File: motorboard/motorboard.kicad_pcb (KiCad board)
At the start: 2 copper layers, 94 x 94 mm, 72 parts, among them J1 Stepper, J2 USB_B_Micro, J3 DC Motor, J4 LiPo, J5 UART, J6 Encoders, J7 ICSP, J8 Separate LiPo, Q1 PMV20ENR, U1 TB6612FNG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

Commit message: forgot something crucial...
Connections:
- U2 pad 28: Net-(U2-Pad28) -> STEP
- U2 pad 29: Net-(U2-Pad29) -> DIR
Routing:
- net STEP: track 0.00 -> 26.3 mm, vias 0 -> 2
- net DIR: track 0.00 -> 24.8 mm, vias 0 -> 2

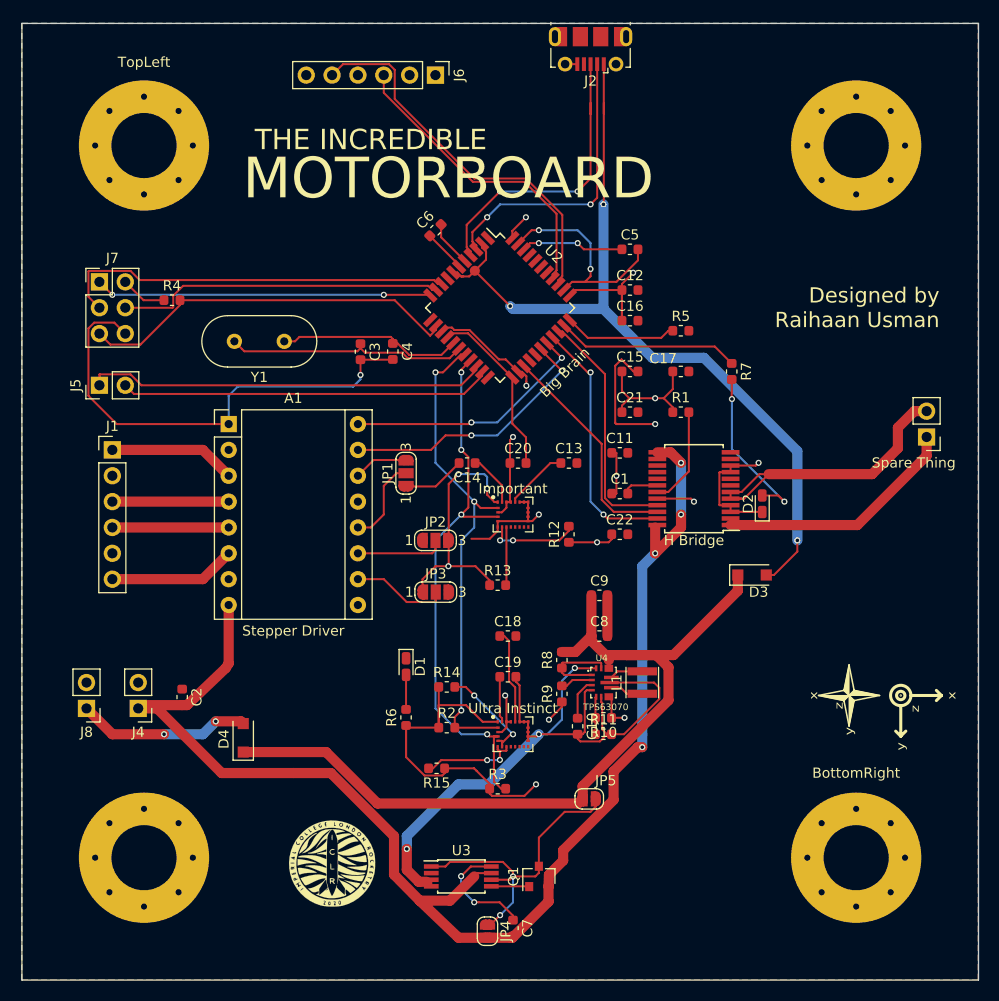
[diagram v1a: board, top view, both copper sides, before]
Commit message: moved things around, looks cleaner
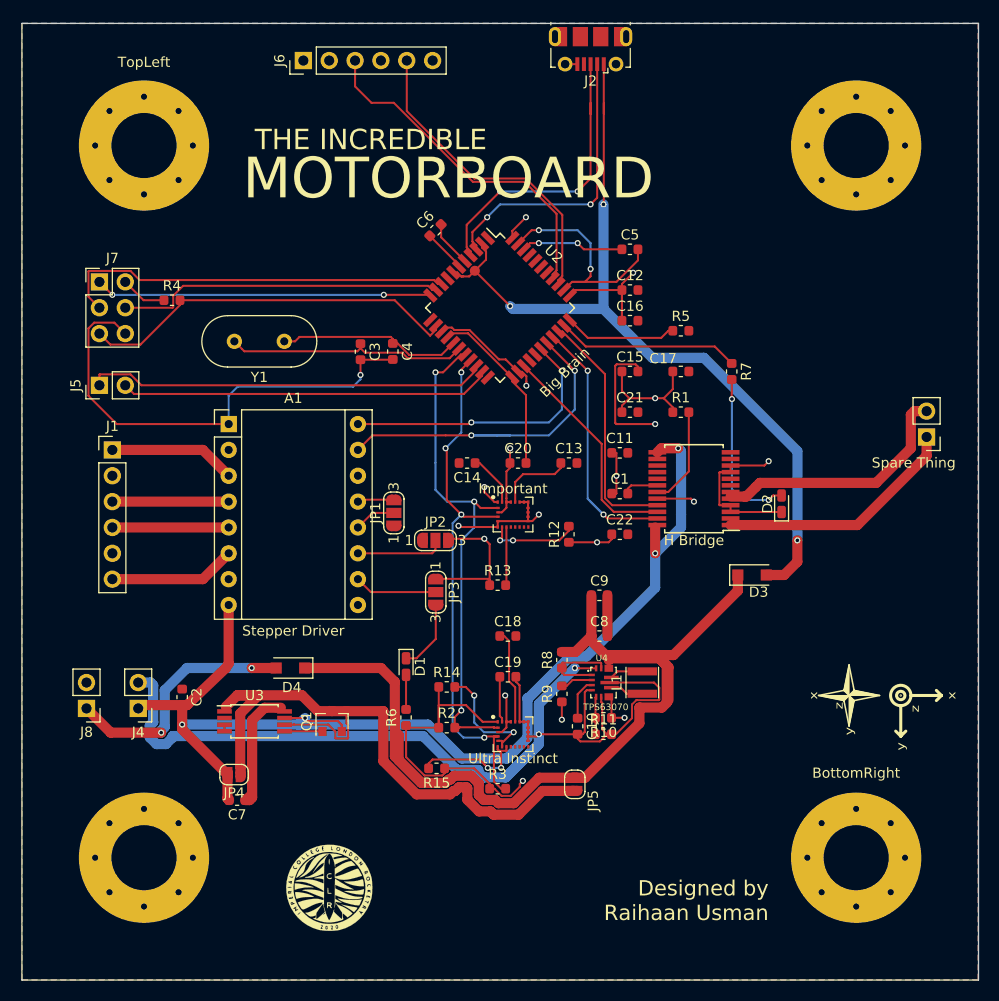
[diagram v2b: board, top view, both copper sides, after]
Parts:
- moved C7 29.9 mm to (116.4, 127.1), turned to 180 degrees
- moved JP4 29.3 mm to (116.1, 124.6), turned to 180 degrees
- moved Q1 25.4 mm to (125.7, 119.4)
- moved U3 25.4 mm to (118.1, 119.4)
- moved J6 13.1 mm to (122.9, 54.5), turned to 90 degrees
- moved D4 8.28 mm to (121.6, 114.1), turned to 180 degrees
- moved JP1 4.08 mm to (131.8, 98.9)
- moved G*** 2.40 mm to (125.5, 135.7)
- moved JP5 2.02 mm to (149.6, 125.6), turned to 270 degrees
- moved D2 1.90 mm to (169.9, 98.0)
- turned JP3 to 270 degrees
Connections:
- U2 pad 28: STEP -> DIR
- U2 pad 29: DIR -> STEP
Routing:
- net Net-(JP4-Pad1): track 31.0 -> 72.5 mm, vias 2 -> 0
- net GND: track 223.4 -> 252.6 mm
- net +15V: track 135.3 -> 113.7 mm
- net VDD: track 86.0 -> 104.4 mm
- net +3V3: track 146.1 -> 132.6 mm, vias 15 -> 14
- net STEP: track 26.3 -> 34.4 mm
- net Net-(C7-Pad1): track 11.3 -> 18.8 mm, vias 2 -> 0
- net Net-(D4-Pad2): track 17.1 -> 24.5 mm
- net A2: track 37.8 -> 31.4 mm
- net AO2: track 30.5 -> 25.3 mm
- net A1: track 30.1 -> 35.2 mm
- net MS3: track 8.59 -> 4.12 mm
- net DIR: track 24.8 -> 27.4 mm
- net PWMA: track 25.1 -> 26.8 mm
- net Net-(R14-Pad2): track 10.4 -> 12.1 mm
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
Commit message: rev2 started
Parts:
- J4: footprint Connector_PinHeader_2.54mm:PinHeader_1x02_P2.54mm_Vertical -> xt30:AMASS_XT30UPB-F_1x02_P5.0mm_Vertical
- moved J8 18.2 mm to (98.8, 100.2)
- moved J4 3.03 mm to (103.9, 119.2), turned to 90 degrees
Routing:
- net GND: track 252.6 -> 234.4 mm, vias 9 -> 10
- net Net-(D4-Pad2): track 24.5 -> 30.2 mm, vias 2 -> 1
- net +15V: track 113.7 -> 117.9 mm
- net Net-(JP4-Pad1): track 72.5 -> 75.9 mm
- net VDD: track 104.4 -> 103.2 mm
- net RST: track 37.7 -> 38.9 mm

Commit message: nicer board!
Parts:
- Y1: footprint Crystal:Crystal_HC18-U_Vertical -> Crystal:Crystal_HC49-4H_Vertical
- moved REF** 2.87 mm to (179.6, 114.8)
- moved REF** 2.87 mm to (174.5, 114.8)
- moved R4 1.38 mm to (110.2, 79.4), turned to 270 degrees
- moved JP3 1.18 mm to (135.9, 105.5), turned to 180 degrees
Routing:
- net Net-(JP4-Pad1): track 75.9 -> 70.6 mm
- net +3V3: track 132.8 -> 128.9 mm, vias 14 -> 15
- net GND: track 234.4 -> 236.8 mm, vias 10 -> 12
- net RST: track 38.9 -> 36.7 mm
- net VDD: track 103.2 -> 101.5 mm
- net MS1: track 8.18 -> 9.19 mm
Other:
- board text added: "Electronics & Payload"
- board text added: "Imperial College London Rocketry"
- board text added: "REV 2"
- board text added: "Redstone Powered..."
- board text added: "The Motorboard is the payload controller designed for HMSS Sporadic Impulse Designed to drive a motor & pulley system to maintain the orientation of the payload cameras!"
- board text added: "What Do I Do?"
- board text removed: "Redstone Powered"

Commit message: Rev2 complete
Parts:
- moved TopLeft 0.21 mm to (107.2, 62.6)
- moved TopRight 0.20 mm to (177.2, 62.6)
- moved BottomLeft 0.19 mm to (107.2, 132.6)
- moved e 0.18 mm to (177.2, 132.6)
- renumbered BottomRight to e
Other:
- outline, holes or cut-outs redrawn
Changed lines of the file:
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@@
   (general
     (thickness 1.6)
-    (drawings 19)
+    (drawings 23)
     (tracks 766)
     (zones 0)
@@
     (mod_text_size 1 1)
     (mod_text_width 0.15)
-    (pad_size 1.524 1.524)
-    (pad_drill 0.762)
+    (pad_size 12.8 12.8)
+    (pad_drill 6.4)
     (pad_to_mask_clearance 0.051)
     (solder_mask_min_width 0.25)
@@
     (uvia_drill 0.1)
   )
+  (module MountingHole:MountingHole_6.4mm_M6_Pad_Via placed (layer F.Cu)
+    (at 177.2 132.6)
+    (descr "Mounting Hole 6.4mm, M6")
+    (tags "mounting hole 6.4mm m6")
+    (attr virtual)
+    (fp_text reference e (at 0 -8.32) (layer F.Fab)
+      (effects (font (size 1 1) (thickness 0.15)))
+    )
+    (fp_text value Yeet (at 0 7.4) (layer F.Fab)
+      (effects (font (size 1 1) (thickness 0.15)))
+    )
+    (fp_text user %R (at 0.3 0) (layer F.Fab)
+      (effects (font (size 1 1) (thickness 0.15)))
+    )
+    (fp_circle (center 0 0) (end 6.4 0) (layer Cmts.User) (width 0.15))
+    (fp_circle (center 0 0) (end 6.65 0) (layer F.CrtYd) (width 0.05))
+    (pad 1 thru_hole circle (at 0 0) (size 12.8 12.8) (drill 6.4) (layers *.Cu *.Mask))
+    (pad 1 thru_hole circle (at 4.8 0) (size 0.9 0.9) (drill 0.6) (layers *.Cu *.Mask))
+    (pad 1 thru_hole circle (at 3.394113 3.394113) (size 0.9 0.9) (drill 0.6) (layers *.Cu *.Mask))
+    (pad 1 thru_hole circle (at 0 4.8) (size 0.9 0.9) (drill 0.6) (layers *.Cu *.Mask))
+    (pad 1 thru_hole circle (at -3.394113 3.394113) (size 0.9 0.9) (drill 0.6) (layers *.Cu *.Mask))
+    (pad 1 thru_hole circle (at -4.8 0) (size 0.9 0.9) (drill 0.6) (layers *.Cu *.Mask))
+    (pad 1 thru_hole circle (at -3.394113 -3.394113) (size 0.9 0.9) (drill 0.6) (layers *.Cu *.Mask))
+    (pad 1 thru_hole circle (at 0 -4.8) (size 0.9 0.9) (drill 0.6) (layers *.Cu *.Mask))
+    (pad 1 thru_hole circle (at 3.394113 -3.394113) (size 0.9 0.9) (drill 0.6) (layers *.Cu *.Mask))
+  )
   (module Crystal:Crystal_HC49-4H_Vertical (layer F.Cu)
     (at 121.031 82.042 180)
@@
   )
   (module MountingHole:MountingHole_6.4mm_M6_Pad_Via placed (layer F.Cu)
-    (at 177.23 132.78)
-    (descr "Mounting Hole 6.4mm, M6")
-    (tags "mounting hole 6.4mm m6")
-    (attr virtual)
-    (fp_text reference BottomRight (at 0 -8.32) (layer F.SilkS)
-      (effects (font (size 1 1) (thickness 0.15)))
-    )
-    (fp_text value Yeet (at 0 7.4) (layer F.Fab)
-      (effects (font (size 1 1) (thickness 0.15)))
-    )
-    (fp_text user %R (at 0.3 0) (layer F.Fab)
-      (effects (font (size 1 1) (thickness 0.15)))
-    )
-    (fp_circle (center 0 0) (end 6.4 0) (layer Cmts.User) (width 0.15))
-    (fp_circle (center 0 0) (end 6.65 0) (layer F.CrtYd) (width 0.05))
-    (pad 1 thru_hole circle (at 0 0) (size 12.8 12.8) (drill 6.4) (layers *.Cu *.Mask))
-    (pad 1 thru_hole circle (at 4.8 0) (size 0.9 0.9) (drill 0.6) (layers *.Cu *.Mask))
-    (pad 1 thru_hole circle (at 3.394113 3.394113) (size 0.9 0.9) (drill 0.6) (layers *.Cu *.Mask))
-    (pad 1 thru_hole circle (at 0 4.8) (size 0.9 0.9) (drill 0.6) (layers *.Cu *.Mask))
-    (pad 1 thru_hole circle (at -3.394113 3.394113) (size 0.9 0.9) (drill 0.6) (layers *.Cu *.Mask))
-    (pad 1 thru_hole circle (at -4.8 0) (size 0.9 0.9) (drill 0.6) (layers *.Cu *.Mask))
-    (pad 1 thru_hole circle (at -3.394113 -3.394113) (size 0.9 0.9) (drill 0.6) (layers *.Cu *.Mask))
-    (pad 1 thru_hole circle (at 0 -4.8) (size 0.9 0.9) (drill 0.6) (layers *.Cu *.Mask))
-    (pad 1 thru_hole circle (at 3.394113 -3.394113) (size 0.9 0.9) (drill 0.6) (layers *.Cu *.Mask))
-  )
-  (module MountingHole:MountingHole_6.4mm_M6_Pad_Via placed (layer F.Cu)
-    (at 177.23 62.8)
+    (at 177.2 62.6)
     (descr "Mounting Hole 6.4mm, M6")
     (tags "mounting hole 6.4mm m6")
@@
   )
   (module MountingHole:MountingHole_6.4mm_M6_Pad_Via placed (layer F.Cu)
-    (at 107.25 62.8)
+    (at 107.2 62.6)
     (descr "Mounting Hole 6.4mm, M6")
     (tags "mounting hole 6.4mm m6")
@@
   )
   (module MountingHole:MountingHole_6.4mm_M6_Pad_Via placed (layer F.Cu)
-    (at 107.25 132.78)
+    (at 107.2 132.6)
     (descr "Mounting Hole 6.4mm, M6")
     (tags "mounting hole 6.4mm m6")
@@
     )
   )
+  (gr_arc (start 107.200001 132.600001) (end 95.200001 132.600001) (angle -90) (layer Edge.Cuts) (width 0.2))
+  (gr_line (start 95.200001 132.600001) (end 95.200001 62.600001) (layer Edge.Cuts) (width 0.2))
+  (gr_line (start 107.200001 50.600001) (end 177.199999 50.600002) (layer Edge.Cuts) (width 0.2))
+  (gr_arc (start 107.200001 62.600002) (end 107.200001 50.600001) (angle -90) (layer Edge.Cuts) (width 0.2))
+  (gr_line (start 177.2 144.6) (end 107.200001 144.600001) (layer Edge.Cuts) (width 0.2))
+  (gr_arc (start 177.199999 62.600002) (end 189.199999 62.600002) (angle -90) (layer Edge.Cuts) (width 0.2))
+  (gr_line (start 189.199999 62.600002) (end 189.2 132.6) (layer Edge.Cuts) (width 0.2))
+  (gr_arc (start 177.2 132.6) (end 177.2 144.6) (angle -90) (layer Edge.Cuts) (width 0.2))
   (gr_text "What Do I Do?" (at 142.468 135.476) (layer B.SilkS)
     (effects (font (size 1.5 1.5) (thickness 0.3)) (justify mirror))
@@
     (effects (font (size 1.5 1.5) (thickness 0.3)) (justify right))
   )
-  (gr_line (start 189.25 144.8) (end 95.25 144.8) (layer Edge.Cuts) (width 0.05))
-  (gr_line (start 189.25 144.8) (end 189.25 50.8) (layer Edge.Cuts) (width 0.05))
-  (gr_line (start 95.25 50.8) (end 189.25 50.8) (layer Edge.Cuts) (width 0.05))
-  (gr_line (start 95.25 50.8) (end 95.25 144.8) (layer Edge.Cuts) (width 0.05))
   (segment (start 144.155 119.425) (end 145.015 119.425) (width 0.2) (layer F.Cu) (net 1) (status 30))
   (segment (start 144.985 119.455) (end 145.015 119.425) (width 0.2) (layer F.Cu) (net 1) (status 30))
@@
   (segment (start 142.341879 122.491879) (end 142.341879 123.532746) (width 0.2) (layer F.Cu) (net 72))
   (segment (start 141.032657 123.95701) (end 142.341879 123.95701) (width 0.2) (layer B.Cu) (net 72))
-  (zone (net 5) (net_name +3V3) (layer B.Cu) (hatch edge 0.508)
+  (zone (net 1) (net_name GND) (layer F.Cu) (hatch edge 0.508)
     (connect_pads (clearance 0.6))
     (min_thickness 0.254)
@@
     (polygon
       (pts
-        (xy 189.23 144.78) (xy 95.25 144.78) (xy 95.25 50.8) (xy 189.23 50.8)
+        (xy 189.2 62.6) (xy 189.2 132.6) (xy 177.2 144.6) (xy 107.2 144.6) (xy 95.2 131.6)
+        (xy 95.2 62.6) (xy 107.2 50.6) (xy 177.2 50.6)
       )
     )
   )
-  (zone (net 1) (net_name GND) (layer F.Cu) (hatch edge 0.508)
+  (zone (net 5) (net_name +3V3) (layer B.Cu) (hatch edge 0.508)
     (connect_pads (clearance 0.6))
     (min_thickness 0.254)
@@
     (polygon
       (pts
-        (xy 189.23 144.78) (xy 95.25 144.78) (xy 95.25 50.8) (xy 189.23 50.8)
+        (xy 189.2 62.6) (xy 189.2 132.6) (xy 177.2 144.6) (xy 107.2 144.6) (xy 95.2 131.6)
+        (xy 95.2 62.6) (xy 107.2 50.6) (xy 177.2 50.6)
       )
     )

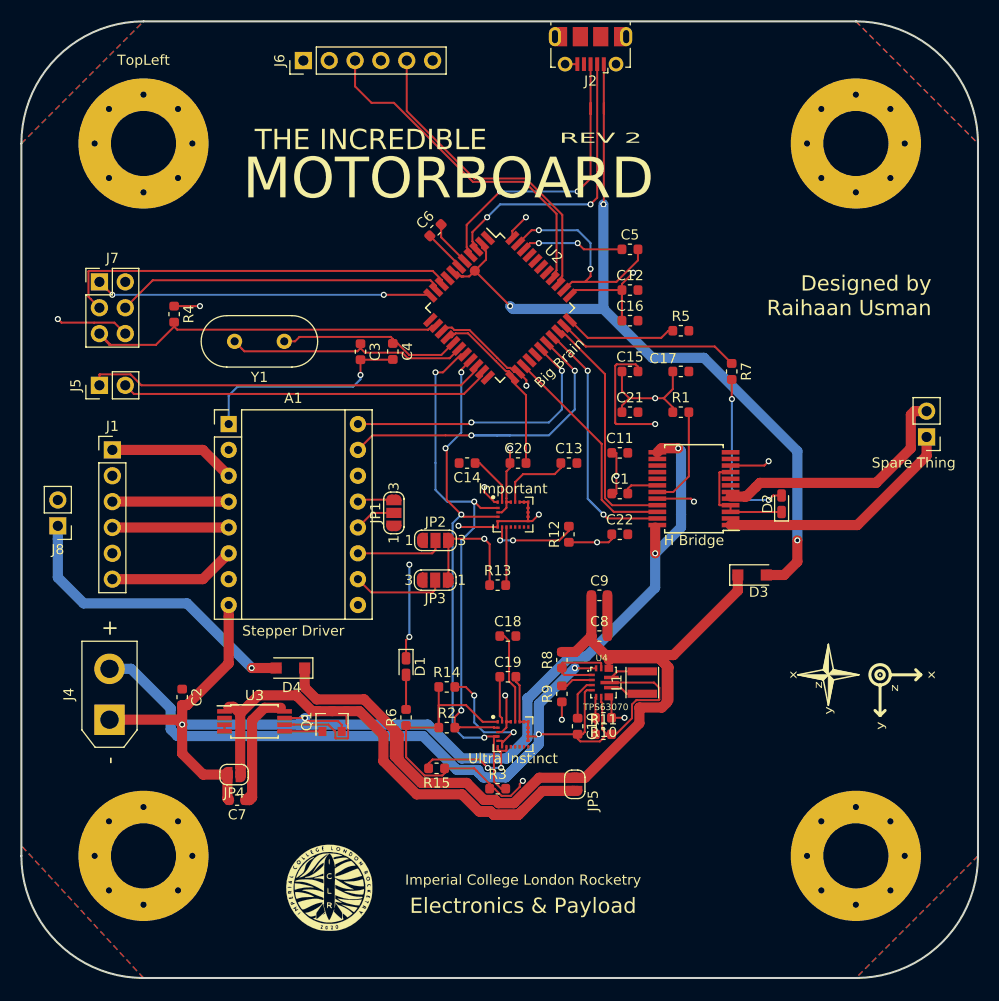
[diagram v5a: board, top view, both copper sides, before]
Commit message: 4 pin header for stepper
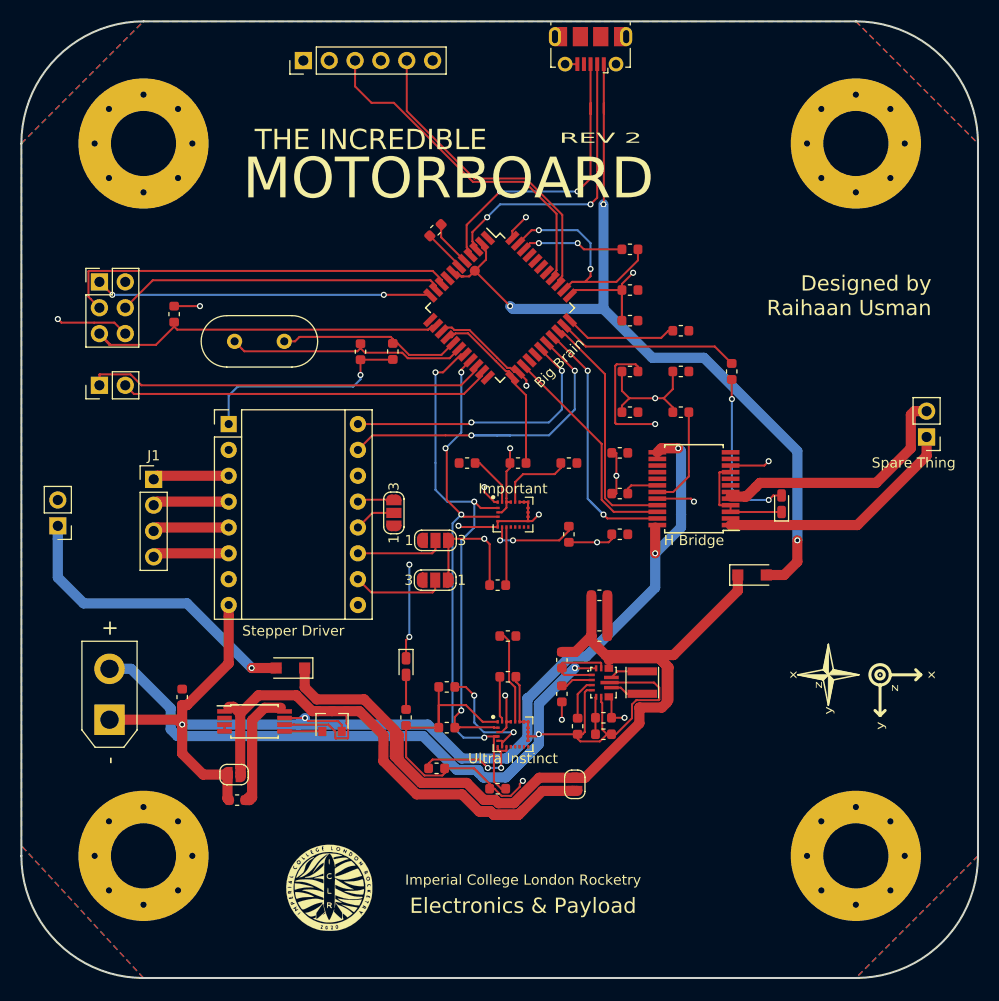
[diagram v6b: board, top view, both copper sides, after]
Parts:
- J1: footprint Connector_PinHeader_2.54mm:PinHeader_1x06_P2.54mm_Vertical -> Connector_PinHeader_2.54mm:PinHeader_1x04_P2.54mm_Vertical
- moved J1 4.98 mm to (108.2, 95.6)
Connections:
- J1 pad 2: Net-(J1-Pad2) -> 1A
- J1 pad 3: 1A -> 2A
- J1 pad 4: 2A -> 2B
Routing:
- net 1B: track 12.5 -> 7.51 mm
- net 2B: track 12.5 -> 7.51 mm
- net 1A: track 11.4 -> 7.51 mm
- net 2A: track 11.4 -> 7.51 mm
